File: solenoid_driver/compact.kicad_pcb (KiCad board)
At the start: 2 copper layers, 51.4 x 58.4 mm, 27 parts, among them J1 Conn_01x02, J2 Conn_01x02, J3 Conn_01x04, J4 Conn_01x02, Q1 IRLZ34N, Q2 IRLZ34N, U1 LM358, U2 L7805

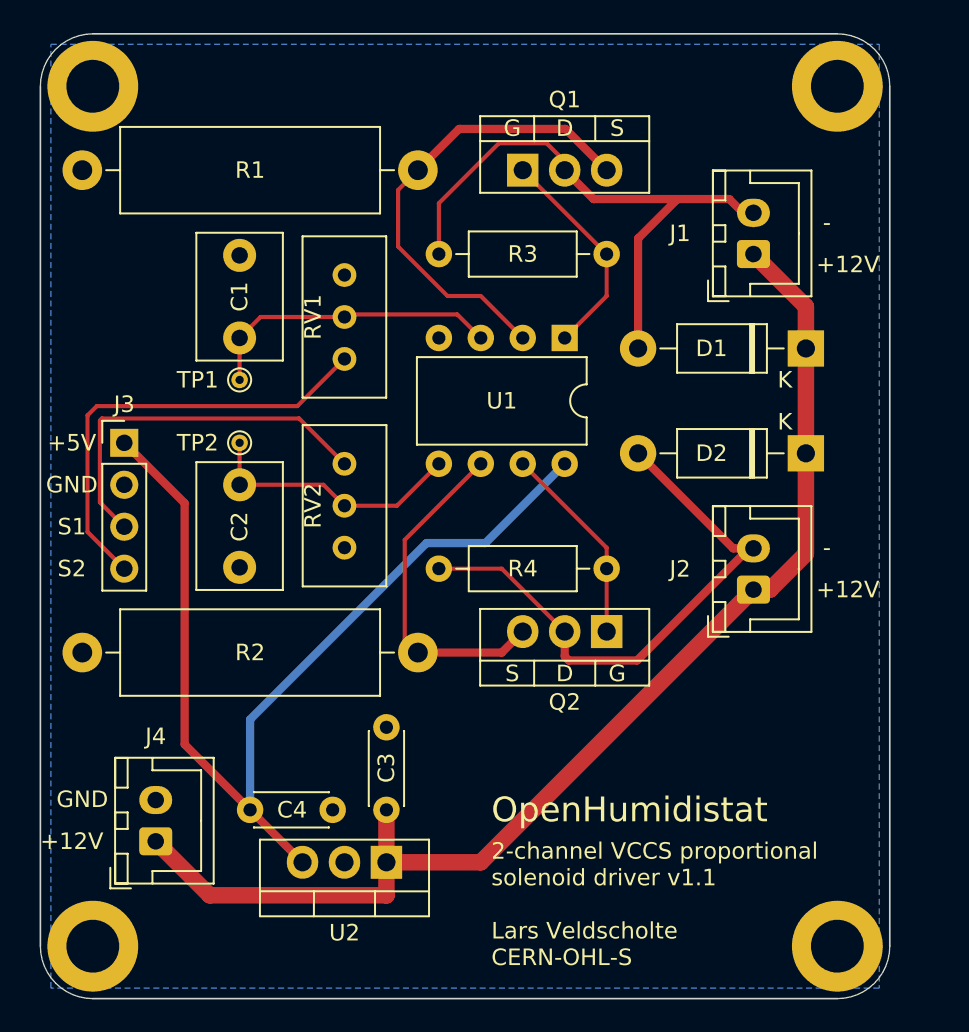
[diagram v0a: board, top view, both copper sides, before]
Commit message: Add fan header to solenoid driver PCB
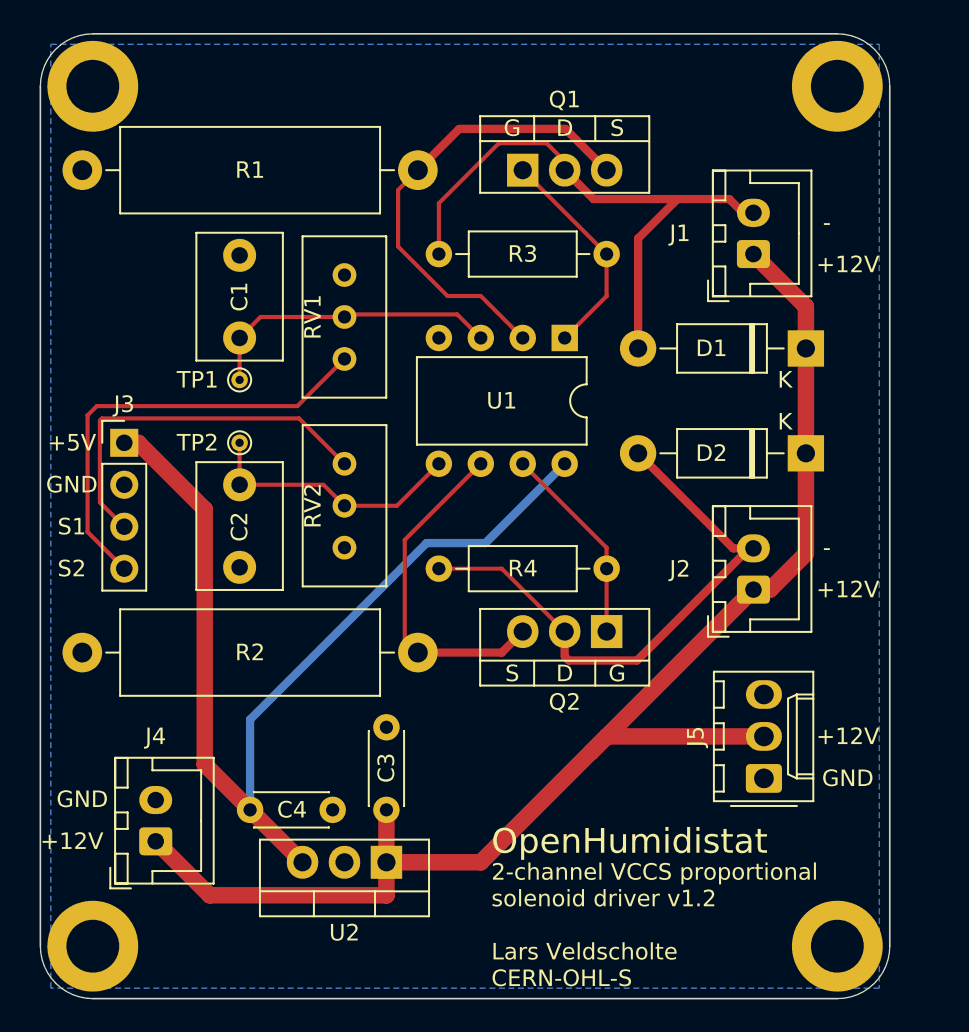
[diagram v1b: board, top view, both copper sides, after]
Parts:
- added J5: Conn_01x03, Connector_Molex:Molex_KK-254_AE-6410-03A_1x03_P2.54mm_Vertical, F.Cu at (78.7, 166.4)
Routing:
- net +12V: track 73.1 -> 84.0 mm
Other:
- board text added: "2-channel VCCS proportional solenoid driver v1.2 Lars Veldscholte CERN-OHL-S"
- board text removed: "2-channel VCCS proportional solenoid driver v1.1 Lars Veldscholte CERN-OHL-S"
